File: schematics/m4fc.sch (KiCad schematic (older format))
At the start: 36 parts

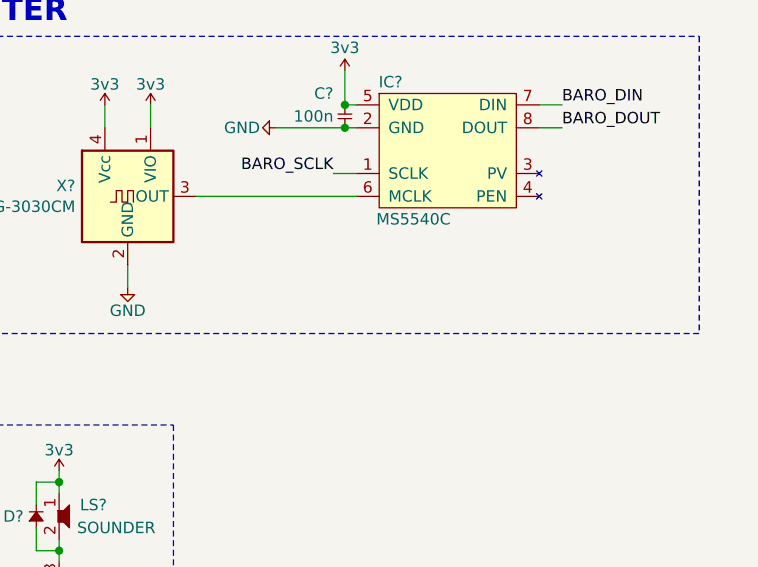
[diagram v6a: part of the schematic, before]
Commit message: Upscale logo resolution and use cusf-kicad for connector symbols
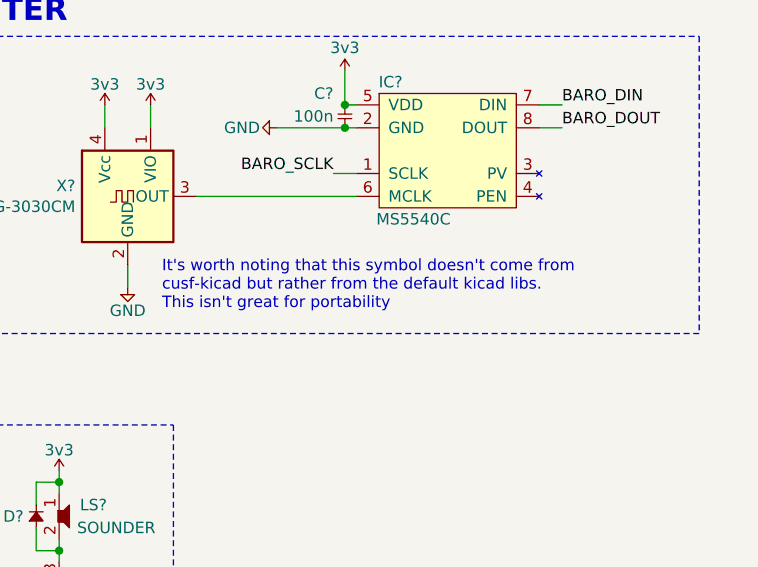
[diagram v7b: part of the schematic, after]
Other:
- note added: "It's worth noting that this symbol doesn't come from\ncusf-kicad but rather from the default kicad libs.\nThis isn't great for portability"
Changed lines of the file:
@@
 U 1 1 5E850CC0
 P 5650 5700
+AR Path="/5E850CC0" Ref="X?"  Part="1"
+AR Path="/6013AEF4/5E850CC0" Ref="X?"  Part="1"
 F 0 "X?" H 5421 5746 50  0000 R CNN
 F 1 "SG-3030CM" H 5421 5655 50  0000 R CNN
@@
 	1    0    0    -1
 $EndComp
+Text Notes 5800 6200 0    50   ~ 0
+It's worth noting that this symbol doesn't come from\ncusf-kicad but rather from the default kicad libs.\nThis isn't great for portability
 $EndSCHEMATC
